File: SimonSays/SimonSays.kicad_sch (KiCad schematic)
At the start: 22 parts, among them X1 Crystal

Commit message: adde
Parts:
- removed S1: cd, Package_DIP:DIP-8_W7.62mm, symbol Analog_Switch:ADG417BN
- removed S2, S3, S4: ADG417BN, Package_DIP:DIP-8_W7.62mm, symbol Analog_Switch:ADG417BN
- added SW1: ws, symbol Switch:SW_Push
- added SW2, SW3, SW4: SW_Push, symbol Switch:SW_Push
- D1: value Blue -> Yellow; footprint (none) -> LED_THT:LED_D3.0mm
- D2: value Yellow -> Blue; footprint (none) -> LED_THT:LED_D3.0mm
- D3: value Red -> Green; footprint (none) -> LED_THT:LED_D3.0mm
- D4: value Green -> Red; footprint (none) -> LED_THT:LED_D3.0mm
- R1, R2, R3, R4, R5, R6, R7, R8: footprint (none) -> Resistor_THT:R_Axial_DIN0207_L6.3mm_D2.5mm_P7.62mm_Horizontal
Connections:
- net GNDREF: now also 5V1.2 (-)
- net at R2.1: now also SW1.2
- net at D1.2 (A): now also UIntegratedCircuit1.11 (PD5); no longer UIntegratedCircuit1.12 (PD6)
- net at 5V1.1 (+), R9.2, UIntegratedCircuit1.7 (VCC): now also UIntegratedCircuit1.20 (AVCC)
- net at UIntegratedCircuit1.5 (PD3): now also SW2.1
- net at R8.1: now also SW4.2
- net at UIntegratedCircuit1.16 (PB2): now also SW4.1
- net at UIntegratedCircuit1.19 (PB5): now also SW3.1
- new net: SW1.1, UIntegratedCircuit1.12 (PD6)

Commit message: Added
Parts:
- R9: footprint (none) -> Resistor_THT:R_Axial_DIN0207_L6.3mm_D2.5mm_P7.62mm_Horizontal
- SW1, SW2, SW3, SW4: footprint (none) -> Button_Switch_THT:SW_TH_Tactile_Omron_B3F-10xx
- renumbered UIntegratedCircuit1 to IntegratedCircuit
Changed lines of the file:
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@@
     (property "Reference" "R9" (id 0) (at 141.224 48.26 90))
     (property "Value" "10K" (id 1) (at 141.224 50.8 90))
-    (property "Footprint" "" (id 2) (at 141.478 53.848 90)
+    (property "Footprint" "Resistor_THT:R_Axial_DIN0207_L6.3mm_D2.5mm_P7.62mm_Horizontal" (id 2) (at 141.478 53.848 90)
       (effects (font (size 1.27 1.27)) hide)
     )
@@
       (effects (font (size 1.27 1.27)) (justify left) hide)
     )
-    (property "Footprint" "" (id 2) (at 190.5 118.618 0)
+    (property "Footprint" "Button_Switch_THT:SW_TH_Tactile_Omron_B3F-10xx" (id 2) (at 190.5 118.618 0)
       (effects (font (size 1.27 1.27)) hide)
     )
@@
       (effects (font (size 1.27 1.27)) (justify left) hide)
     )
-    (property "Footprint" "" (id 2) (at 166.116 118.618 0)
+    (property "Footprint" "Button_Switch_THT:SW_TH_Tactile_Omron_B3F-10xx" (id 2) (at 166.116 118.618 0)
       (effects (font (size 1.27 1.27)) hide)
     )
@@
       (effects (font (size 1.27 1.27)) (justify left) hide)
     )
-    (property "Footprint" "" (id 2) (at 142.24 119.38 0)
+    (property "Footprint" "Button_Switch_THT:SW_TH_Tactile_Omron_B3F-10xx" (id 2) (at 142.24 119.38 0)
       (effects (font (size 1.27 1.27)) hide)
     )
@@
       (effects (font (size 1.27 1.27)) (justify left) hide)
     )
-    (property "Footprint" "" (id 2) (at 117.856 120.142 0)
+    (property "Footprint" "Button_Switch_THT:SW_TH_Tactile_Omron_B3F-10xx" (id 2) (at 117.856 120.142 0)
       (effects (font (size 1.27 1.27)) hide)
     )
@@
   (symbol (lib_id "MCU_Microchip_ATmega:ATmega328-P") (at 143.256 71.374 270) (unit 1)
     (in_bom yes) (on_board yes) (fields_autoplaced)
-    (property "Reference" "UIntegratedCircuit1" (id 0) (at 176.5047 53.34 90)
+    (property "Reference" "IntegratedCircuit" (id 0) (at 176.5047 53.34 90)
       (effects (font (size 1.27 1.27)) (justify left))
     )
@@
       (reference "D4") (unit 1) (value "Red") (footprint "LED_THT:LED_D3.0mm")
     )
+    (path "/f5606098-a4b5-4eeb-9fa5-f9d99a2e7a01"
+      (reference "IntegratedCircuit") (unit 1) (value "ATmega328-P") (footprint "Package_DIP:DIP-28_W7.62mm")
+    )
     (path "/e962bc73-4e3b-4fbe-90ec-ef049ff02d8b"
       (reference "R1") (unit 1) (value "10k") (footprint "Resistor_THT:R_Axial_DIN0207_L6.3mm_D2.5mm_P7.62mm_Horizontal")
@@
     )
     (path "/228059e3-e3c4-46b3-ad02-441c163a776b"
-      (reference "R9") (unit 1) (value "10K") (footprint "")
+      (reference "R9") (unit 1) (value "10K") (footprint "Resistor_THT:R_Axial_DIN0207_L6.3mm_D2.5mm_P7.62mm_Horizontal")
     )
     (path "/8f68f853-0400-4a27-967f-ab868c4f04dd"
-      (reference "SW1") (unit 1) (value "ws") (footprint "")
+      (reference "SW1") (unit 1) (value "ws") (footprint "Button_Switch_THT:SW_TH_Tactile_Omron_B3F-10xx")
     )
     (path "/4b6b1196-6d1d-4776-a754-4c16c447bf4d"
-      (reference "SW2") (unit 1) (value "SW_Push") (footprint "")
+      (reference "SW2") (unit 1) (value "SW_Push") (footprint "Button_Switch_THT:SW_TH_Tactile_Omron_B3F-10xx")
     )
     (path "/402307f2-18fd-4edb-b9fd-0ddb66313638"
-      (reference "SW3") (unit 1) (value "SW_Push") (footprint "")
+      (reference "SW3") (unit 1) (value "SW_Push") (footprint "Button_Switch_THT:SW_TH_Tactile_Omron_B3F-10xx")
     )
     (path "/2bd2fde5-740a-47d2-ae92-3a92e886fd42"
-      (reference "SW4") (unit 1) (value "SW_Push") (footprint "")
-    )
-    (path "/f5606098-a4b5-4eeb-9fa5-f9d99a2e7a01"
-      (reference "UIntegratedCircuit1") (unit 1) (value "ATmega328-P") (footprint "Package_DIP:DIP-28_W7.62mm")
+      (reference "SW4") (unit 1) (value "SW_Push") (footprint "Button_Switch_THT:SW_TH_Tactile_Omron_B3F-10xx")
     )
     (path "/83e3b593-8bcf-44c4-82ef-5843b2b698b8"

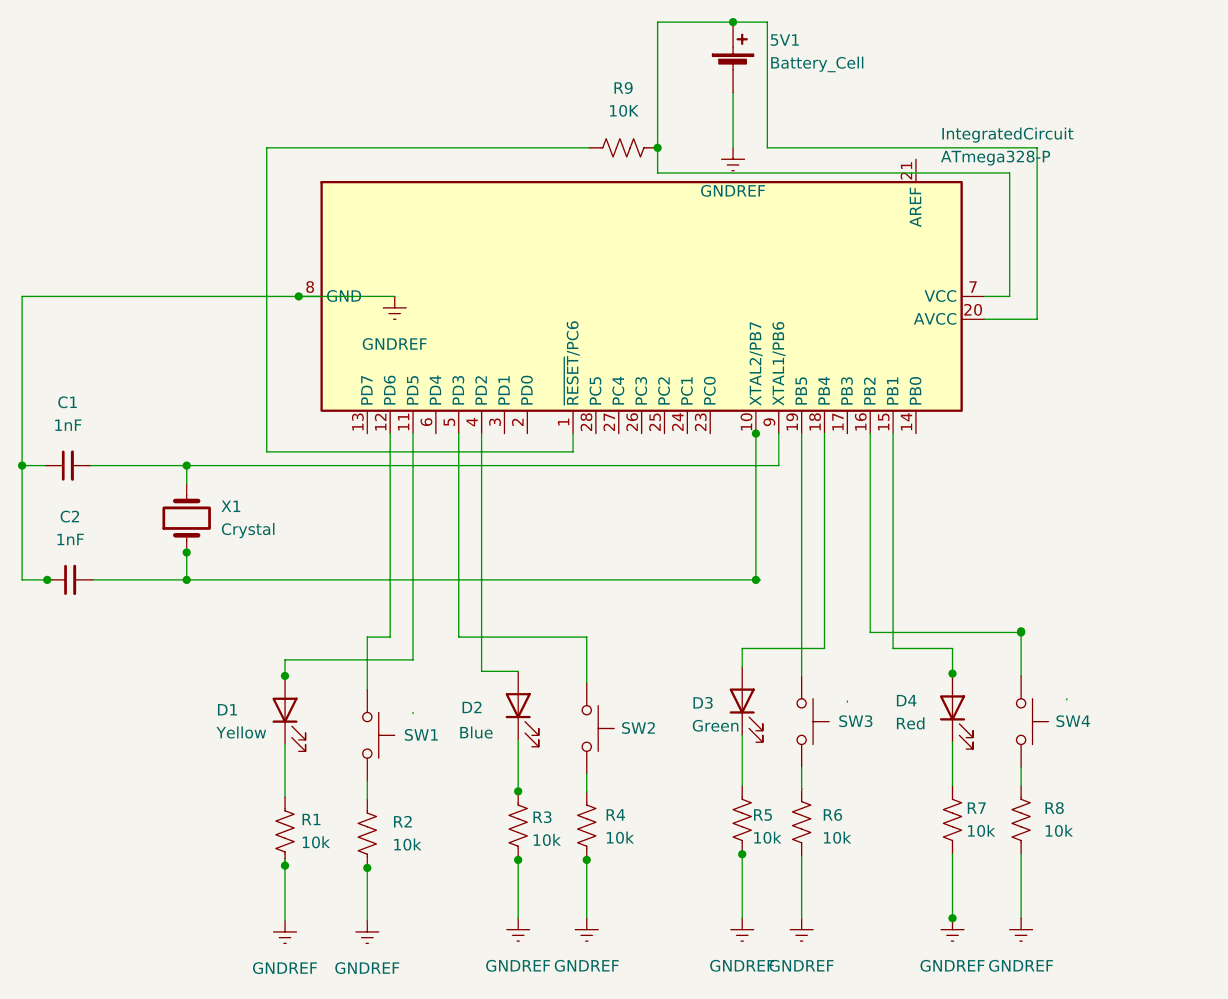
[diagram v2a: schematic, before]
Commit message: clean up wires
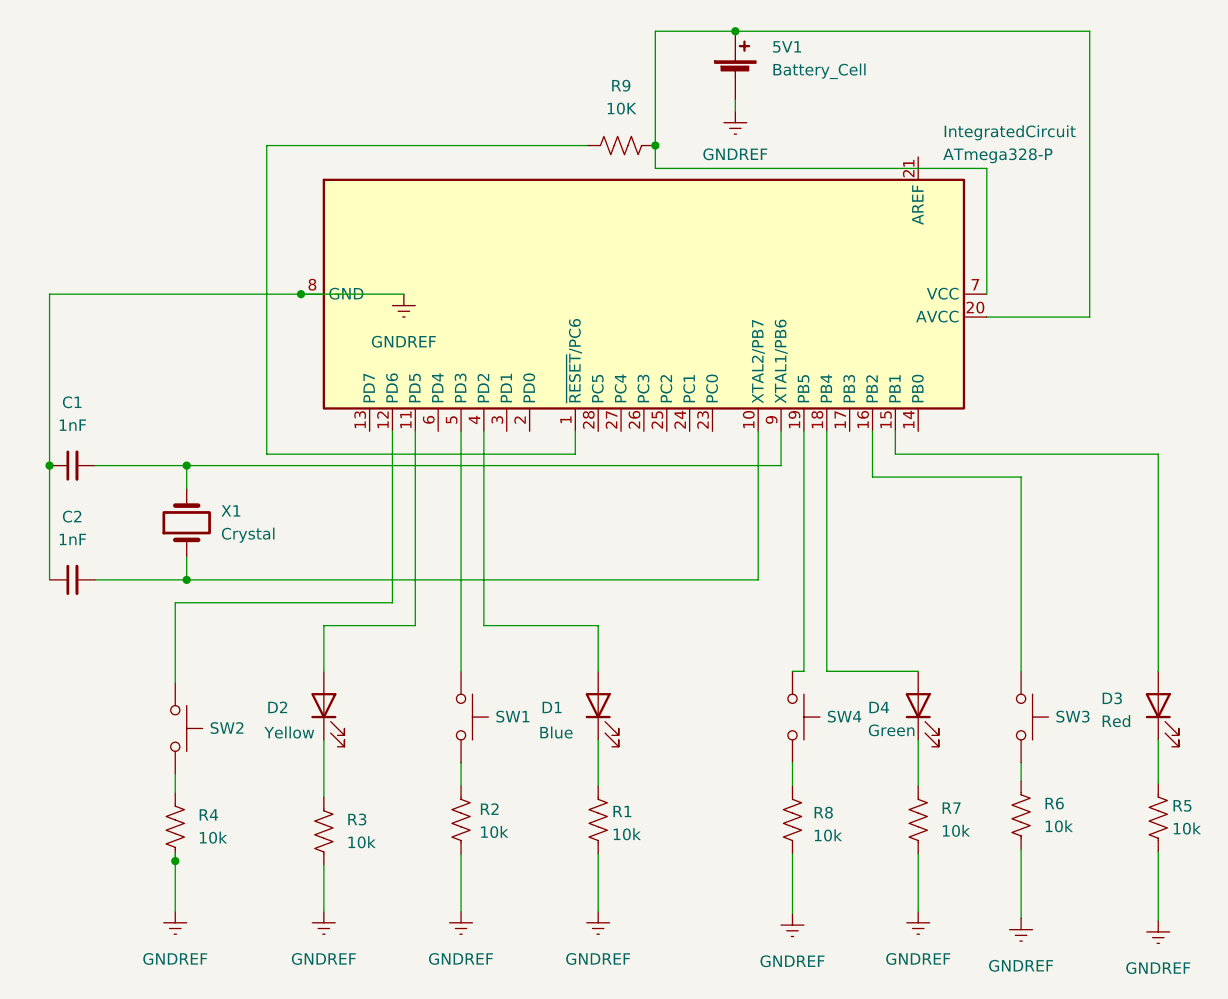
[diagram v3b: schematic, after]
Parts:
- removed D1: Yellow, LED_THT:LED_D3.0mm, symbol Device:LED
- removed R5: 10k, Resistor_THT:R_Axial_DIN0207_L6.3mm_D2.5mm_P7.62mm_Horizontal, symbol Device:R_US
- added D2: Yellow, LED_THT:LED_D3.0mm, symbol Device:LED
- added R7: 10k, Resistor_THT:R_Axial_DIN0207_L6.3mm_D2.5mm_P7.62mm_Horizontal, symbol Device:R_US
- renumbered D2 to D1, D4 to D3, D3 to D4, R3 to R1, R4 to R2, R1 to R3, R2 to R4, R7 to R5, R8 to R6, R6 to R8, SW2 to SW1, SW1 to SW2, SW4 to SW3, SW3 to SW4
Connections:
- net GNDREF: now also R7.2
- net at R3.1: now also D2.1 (K)
- net at IntegratedCircuit.11 (PD5): now also D2.2 (A)
- net at R2.1: now also SW1.2
- net at D4.1 (K): now also R7.1
- net at R8.1: now also SW4.2
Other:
- title: (none) -> Simon Says
- moved on the sheet: 5V1, C1, D1, D3, D4, R1, R2, R3, R4, R5, R6, R8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

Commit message: clean footprints
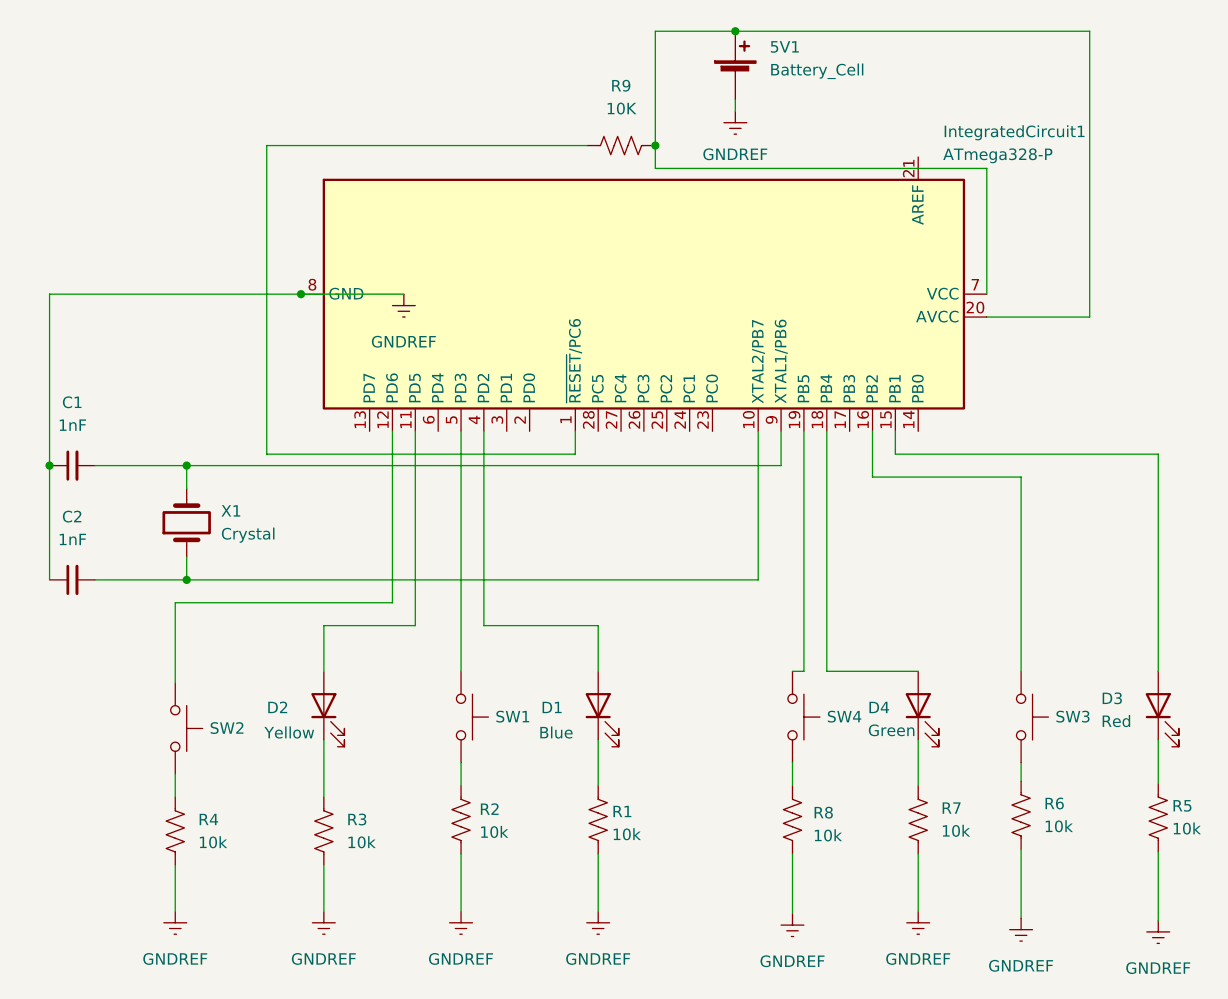
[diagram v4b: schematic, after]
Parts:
- C1, C2: footprint Capacitor_THT:CP_Axial_L10.0mm_D4.5mm_P15.00mm_Horizontal -> Capacitor_THT:CP_Radial_D4.0mm_P1.50mm
- SW2: value ws -> SW_Push
- X1: footprint Crystal:Crystal_HC18-U_Vertical -> Crystal:Crystal_HC49-4H_Vertical
- renumbered IntegratedCircuit to IntegratedCircuit1
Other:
- moved on the sheet: R4
